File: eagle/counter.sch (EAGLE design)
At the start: 11 parts

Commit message: Update schematic
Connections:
- new net N$11: ARDUINO_MINI.5, XBEE.DOUT
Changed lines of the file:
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@@
+</segment>
+</net>
+<net name="N$11" class="0">
+<segment>
+<pinref part="ARDUINO_MINI" gate="G$1" pin="5"/>
+<wire x1="88.9" y1="71.12" x2="76.2" y2="71.12" width="0.2032" layer="91"/>
+<wire x1="76.2" y1="71.12" x2="76.2" y2="66.04" width="0.2032" layer="91"/>
+<pinref part="XBEE" gate="G$1" pin="DOUT"/>
+<wire x1="76.2" y1="66.04" x2="71.12" y2="66.04" width="0.2032" layer="91"/>
+<junction x="71.12" y="66.04"/>
+<junction x="88.9" y="71.12"/>
 </segment>
 </net>

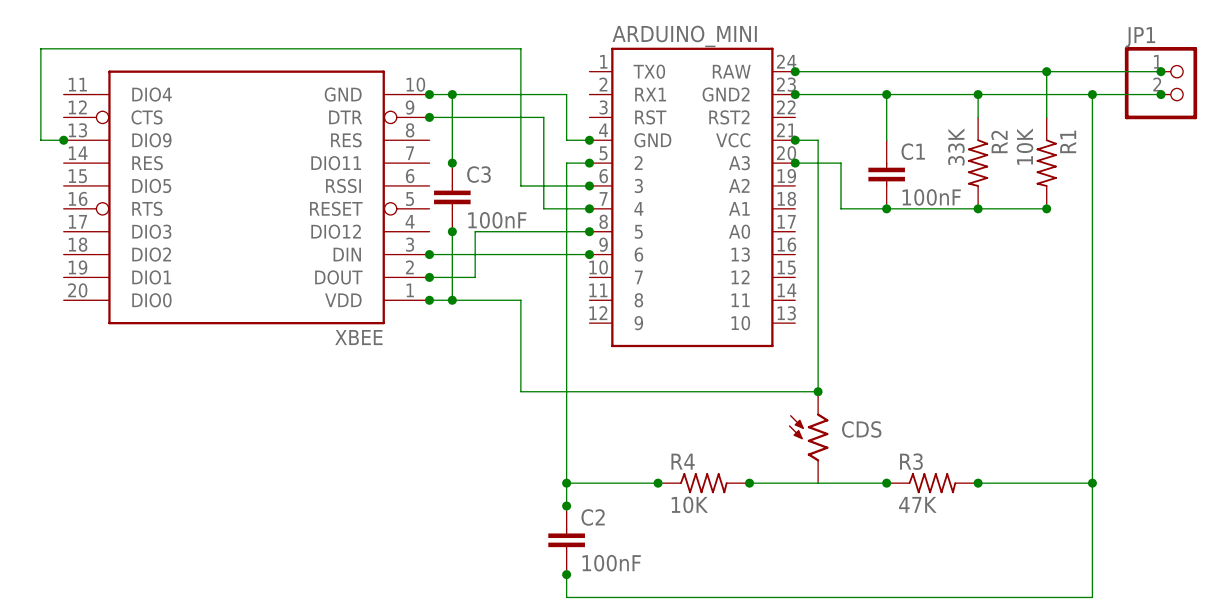
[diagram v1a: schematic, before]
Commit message: Moving debug code to header, cleaning up and some minor changes
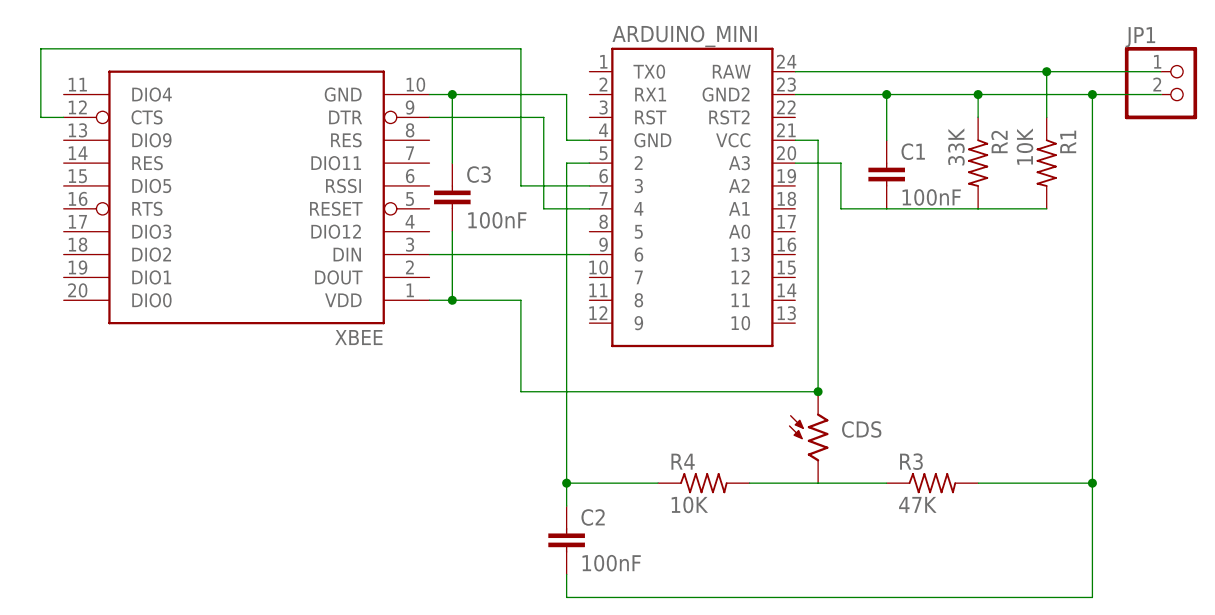
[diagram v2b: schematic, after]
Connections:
- removed net N$11: ARDUINO_MINI.5, XBEE.DOUT
- net N$10: now also XBEE.CTS; no longer XBEE.DIO9
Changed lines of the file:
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@@
 <pinref part="XBEE" gate="G$1" pin="GND"/>
 <wire x1="86.36" y1="86.36" x2="73.66" y2="86.36" width="0.2032" layer="91"/>
-<junction x="71.12" y="86.36"/>
-<junction x="88.9" y="81.28"/>
 <pinref part="C3" gate="G$1" pin="1"/>
 <wire x1="73.66" y1="86.36" x2="71.12" y2="86.36" width="0.2032" layer="91"/>
 <wire x1="73.66" y1="78.74" x2="73.66" y2="86.36" width="0.2032" layer="91"/>
 <junction x="73.66" y="86.36"/>
-<junction x="73.66" y="78.74"/>
 </segment>
 </net>
@@
 <wire x1="114.3" y1="81.28" x2="114.3" y2="53.34" width="0.2032" layer="91"/>
 <pinref part="CDS" gate="G$1" pin="1"/>
-<junction x="111.76" y="81.28"/>
 <pinref part="XBEE" gate="G$1" pin="VDD"/>
 <wire x1="71.12" y1="63.5" x2="73.66" y2="63.5" width="0.2032" layer="91"/>
@@
 <wire x1="81.28" y1="63.5" x2="81.28" y2="53.34" width="0.2032" layer="91"/>
 <wire x1="81.28" y1="53.34" x2="114.3" y2="53.34" width="0.2032" layer="91"/>
-<junction x="71.12" y="63.5"/>
 <junction x="114.3" y="53.34"/>
 <pinref part="C3" gate="G$1" pin="2"/>
 <wire x1="73.66" y1="71.12" x2="73.66" y2="63.5" width="0.2032" layer="91"/>
-<junction x="73.66" y="71.12"/>
 <junction x="73.66" y="63.5"/>
 </segment>
@@
 <wire x1="139.7" y1="83.82" x2="139.7" y2="88.9" width="0.2032" layer="91"/>
 <junction x="139.7" y="88.9"/>
-<junction x="111.76" y="88.9"/>
-<junction x="152.4" y="88.9"/>
 </segment>
 </net>
@@
 <wire x1="144.78" y1="43.18" x2="144.78" y2="86.36" width="0.2032" layer="91"/>
 <junction x="144.78" y="86.36"/>
-<junction x="111.76" y="86.36"/>
-<junction x="152.4" y="86.36"/>
-<junction x="132.08" y="43.18"/>
 <pinref part="C2" gate="G$1" pin="2"/>
 <wire x1="86.36" y1="33.02" x2="86.36" y2="30.48" width="0.2032" layer="91"/>
@@
 <wire x1="144.78" y1="30.48" x2="144.78" y2="43.18" width="0.2032" layer="91"/>
 <junction x="144.78" y="43.18"/>
-<junction x="86.36" y="33.02"/>
 </segment>
 </net>
@@
 <pinref part="ARDUINO_MINI" gate="G$1" pin="A3"/>
 <wire x1="116.84" y1="78.74" x2="111.76" y2="78.74" width="0.2032" layer="91"/>
-<junction x="111.76" y="78.74"/>
-<junction x="121.92" y="73.66"/>
 <pinref part="R2" gate="G$1" pin="2"/>
-<junction x="132.08" y="73.66"/>
-<junction x="139.7" y="73.66"/>
 </segment>
 </net>
@@
 <pinref part="ARDUINO_MINI" gate="G$1" pin="2"/>
 <wire x1="86.36" y1="78.74" x2="88.9" y2="78.74" width="0.2032" layer="91"/>
-<junction x="88.9" y="78.74"/>
 <pinref part="R4" gate="G$1" pin="1"/>
 <wire x1="96.52" y1="43.18" x2="86.36" y2="43.18" width="0.2032" layer="91"/>
 <wire x1="86.36" y1="43.18" x2="86.36" y2="78.74" width="0.2032" layer="91"/>
-<junction x="96.52" y="43.18"/>
 <pinref part="C2" gate="G$1" pin="1"/>
 <wire x1="86.36" y1="43.18" x2="86.36" y2="40.64" width="0.2032" layer="91"/>
-<junction x="86.36" y="40.64"/>
 <junction x="86.36" y="43.18"/>
 </segment>
@@
 <pinref part="ARDUINO_MINI" gate="G$1" pin="4"/>
 <wire x1="83.82" y1="73.66" x2="88.9" y2="73.66" width="0.2032" layer="91"/>
-<junction x="71.12" y="83.82"/>
-<junction x="88.9" y="73.66"/>
 </segment>
 </net>
@@
 <pinref part="CDS" gate="G$1" pin="2"/>
 <pinref part="R3" gate="G$1" pin="1"/>
-<junction x="121.92" y="43.18"/>
 <wire x1="121.92" y1="43.18" x2="114.3" y2="43.18" width="0.2032" layer="91"/>
 <pinref part="R4" gate="G$1" pin="2"/>
 <wire x1="114.3" y1="43.18" x2="106.68" y2="43.18" width="0.2032" layer="91"/>
-<junction x="106.68" y="43.18"/>
 </segment>
 </net>
@@
 <pinref part="ARDUINO_MINI" gate="G$1" pin="6"/>
 <wire x1="71.12" y1="68.58" x2="88.9" y2="68.58" width="0.2032" layer="91"/>
-<junction x="71.12" y="68.58"/>
-<junction x="88.9" y="68.58"/>
 </segment>
 </net>
 <net name="N$10" class="0">
 <segment>
-<pinref part="XBEE" gate="G$1" pin="DIO9"/>
-<wire x1="30.48" y1="81.28" x2="27.94" y2="81.28" width="0.2032" layer="91"/>
-<wire x1="27.94" y1="81.28" x2="27.94" y2="91.44" width="0.2032" layer="91"/>
 <wire x1="27.94" y1="91.44" x2="81.28" y2="91.44" width="0.2032" layer="91"/>
 <wire x1="81.28" y1="91.44" x2="81.28" y2="76.2" width="0.2032" layer="91"/>
 <pinref part="ARDUINO_MINI" gate="G$1" pin="3"/>
 <wire x1="81.28" y1="76.2" x2="88.9" y2="76.2" width="0.2032" layer="91"/>
-<junction x="88.9" y="76.2"/>
-<junction x="30.48" y="81.28"/>
+<wire x1="27.94" y1="91.44" x2="27.94" y2="83.82" width="0.2032" layer="91"/>
+<pinref part="XBEE" gate="G$1" pin="CTS"/>
+<wire x1="27.94" y1="83.82" x2="30.48" y2="83.82" width="0.2032" layer="91"/>
 </segment>
 </net>
-<net name="N$11" class="0">
-<segment>
-<pinref part="ARDUINO_MINI" gate="G$1" pin="5"/>
-<wire x1="88.9" y1="71.12" x2="76.2" y2="71.12" width="0.2032" layer="91"/>
-<wire x1="76.2" y1="71.12" x2="76.2" y2="66.04" width="0.2032" layer="91"/>
-<pinref part="XBEE" gate="G$1" pin="DOUT"/>
-<wire x1="76.2" y1="66.04" x2="71.12" y2="66.04" width="0.2032" layer="91"/>
-<junction x="71.12" y="66.04"/>
-<junction x="88.9" y="71.12"/>
-</segment>
-</net>

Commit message: Update files and license
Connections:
- net N$10: now also XBEE.DIO9; no longer XBEE.CTS
- net N$9: now also ARDUINO_MINI.TX0; no longer ARDUINO_MINI.6
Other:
- moved on the sheet: C3, XBEE
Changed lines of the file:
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@@
 <instances>
 <instance part="ARDUINO_MINI" gate="G$1" x="99.06" y="76.2"/>
-<instance part="XBEE" gate="G$1" x="50.8" y="73.66" rot="R180"/>
+<instance part="XBEE" gate="G$1" x="48.26" y="73.66" rot="R180"/>
 <instance part="R1" gate="G$1" x="139.7" y="78.74" rot="R270"/>
 <instance part="R2" gate="G$1" x="132.08" y="78.74" rot="R270"/>
@@
 <instance part="R4" gate="G$1" x="101.6" y="43.18"/>
 <instance part="C2" gate="G$1" x="86.36" y="38.1"/>
-<instance part="C3" gate="G$1" x="73.66" y="76.2"/>
+<instance part="C3" gate="G$1" x="71.12" y="76.2"/>
 </instances>
 <busses>
@@
 <wire x1="86.36" y1="81.28" x2="86.36" y2="86.36" width="0.2032" layer="91"/>
 <pinref part="XBEE" gate="G$1" pin="GND"/>
-<wire x1="86.36" y1="86.36" x2="73.66" y2="86.36" width="0.2032" layer="91"/>
+<wire x1="86.36" y1="86.36" x2="71.12" y2="86.36" width="0.2032" layer="91"/>
 <pinref part="C3" gate="G$1" pin="1"/>
-<wire x1="73.66" y1="86.36" x2="71.12" y2="86.36" width="0.2032" layer="91"/>
-<wire x1="73.66" y1="78.74" x2="73.66" y2="86.36" width="0.2032" layer="91"/>
-<junction x="73.66" y="86.36"/>
+<wire x1="71.12" y1="86.36" x2="68.58" y2="86.36" width="0.2032" layer="91"/>
+<wire x1="71.12" y1="78.74" x2="71.12" y2="86.36" width="0.2032" layer="91"/>
+<junction x="71.12" y="86.36"/>
 </segment>
 </net>
@@
 <pinref part="CDS" gate="G$1" pin="1"/>
 <pinref part="XBEE" gate="G$1" pin="VDD"/>
-<wire x1="71.12" y1="63.5" x2="73.66" y2="63.5" width="0.2032" layer="91"/>
-<wire x1="73.66" y1="63.5" x2="81.28" y2="63.5" width="0.2032" layer="91"/>
+<wire x1="68.58" y1="63.5" x2="71.12" y2="63.5" width="0.2032" layer="91"/>
+<wire x1="71.12" y1="63.5" x2="81.28" y2="63.5" width="0.2032" layer="91"/>
 <wire x1="81.28" y1="63.5" x2="81.28" y2="53.34" width="0.2032" layer="91"/>
 <wire x1="81.28" y1="53.34" x2="114.3" y2="53.34" width="0.2032" layer="91"/>
 <junction x="114.3" y="53.34"/>
 <pinref part="C3" gate="G$1" pin="2"/>
-<wire x1="73.66" y1="71.12" x2="73.66" y2="63.5" width="0.2032" layer="91"/>
-<junction x="73.66" y="63.5"/>
+<wire x1="71.12" y1="71.12" x2="71.12" y2="63.5" width="0.2032" layer="91"/>
+<junction x="71.12" y="63.5"/>
 </segment>
 </net>
@@
 <segment>
 <pinref part="XBEE" gate="G$1" pin="DTR"/>
-<wire x1="71.12" y1="83.82" x2="83.82" y2="83.82" width="0.2032" layer="91"/>
+<wire x1="68.58" y1="83.82" x2="83.82" y2="83.82" width="0.2032" layer="91"/>
 <wire x1="83.82" y1="83.82" x2="83.82" y2="73.66" width="0.2032" layer="91"/>
 <pinref part="ARDUINO_MINI" gate="G$1" pin="4"/>
@@
 </segment>
 </net>
+<net name="N$10" class="0">
+<segment>
+<wire x1="25.4" y1="91.44" x2="81.28" y2="91.44" width="0.2032" layer="91"/>
+<wire x1="81.28" y1="91.44" x2="81.28" y2="76.2" width="0.2032" layer="91"/>
+<pinref part="ARDUINO_MINI" gate="G$1" pin="3"/>
+<wire x1="81.28" y1="76.2" x2="88.9" y2="76.2" width="0.2032" layer="91"/>
+<wire x1="25.4" y1="91.44" x2="25.4" y2="81.28" width="0.2032" layer="91"/>
+<pinref part="XBEE" gate="G$1" pin="DIO9"/>
+<wire x1="25.4" y1="81.28" x2="27.94" y2="81.28" width="0.2032" layer="91"/>
+</segment>
+</net>
 <net name="N$9" class="0">
 <segment>
 <pinref part="XBEE" gate="G$1" pin="DIN"/>
-<pinref part="ARDUINO_MINI" gate="G$1" pin="6"/>
-<wire x1="71.12" y1="68.58" x2="88.9" y2="68.58" width="0.2032" layer="91"/>
+<wire x1="68.58" y1="68.58" x2="78.74" y2="68.58" width="0.2032" layer="91"/>
+<wire x1="78.74" y1="68.58" x2="78.74" y2="88.9" width="0.2032" layer="91"/>
+<pinref part="ARDUINO_MINI" gate="G$1" pin="TX0"/>
+<wire x1="78.74" y1="88.9" x2="88.9" y2="88.9" width="0.2032" layer="91"/>
 </segment>
 </net>
-<net name="N$10" class="0">
-<segment>
-<wire x1="27.94" y1="91.44" x2="81.28" y2="91.44" width="0.2032" layer="91"/>
-<wire x1="81.28" y1="91.44" x2="81.28" y2="76.2" width="0.2032" layer="91"/>
-<pinref part="ARDUINO_MINI" gate="G$1" pin="3"/>
-<wire x1="81.28" y1="76.2" x2="88.9" y2="76.2" width="0.2032" layer="91"/>
-<wire x1="27.94" y1="91.44" x2="27.94" y2="83.82" width="0.2032" layer="91"/>
-<pinref part="XBEE" gate="G$1" pin="CTS"/>
-<wire x1="27.94" y1="83.82" x2="30.48" y2="83.82" width="0.2032" layer="91"/>
-</segment>
-</net>
